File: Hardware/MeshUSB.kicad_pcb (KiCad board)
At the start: 2 copper layers, 30.4 x 40.8 mm, 33 parts, among them P1 USB_4, P2 PVCell, Q1 MOS_P, U1 XBEE, U2 AP7313-3.3VREGULATOR, U4 FT231X-SSOP, U5 LTC4070

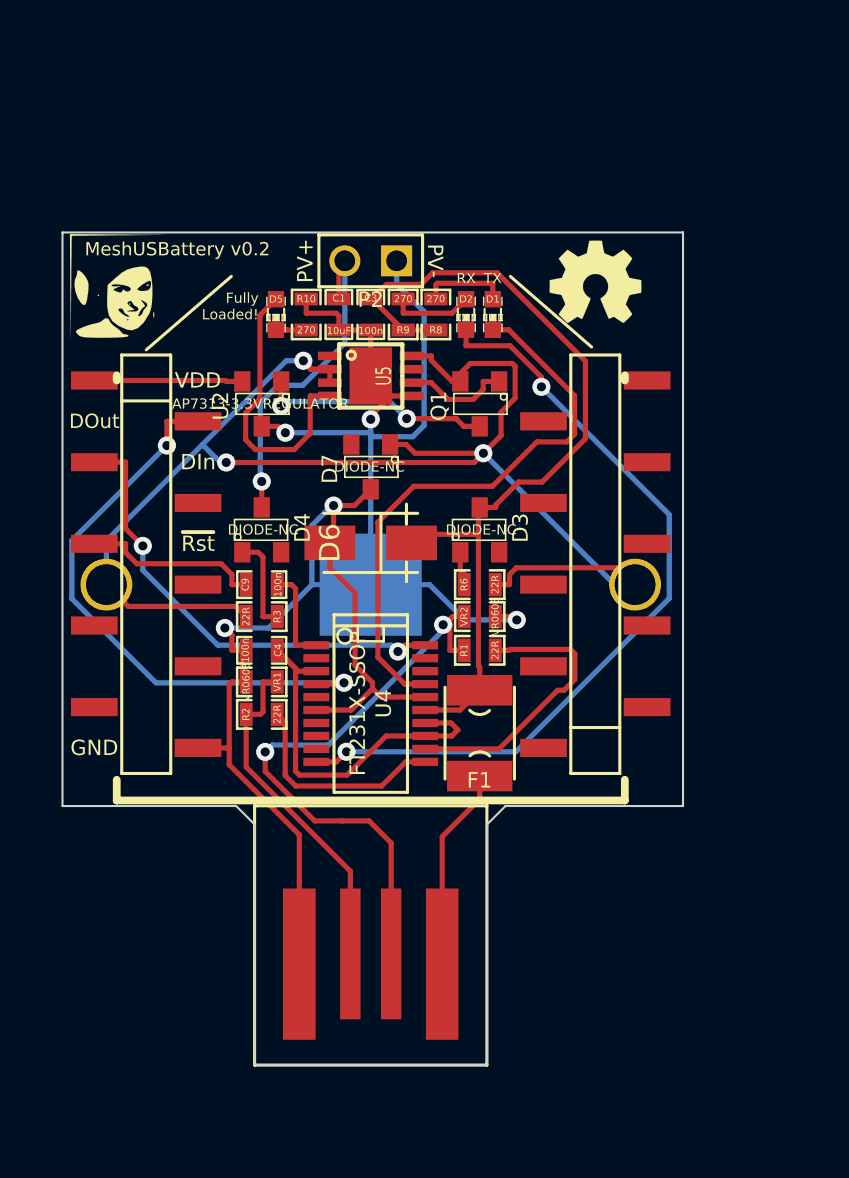
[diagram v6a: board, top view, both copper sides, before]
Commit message: Added mounting holes, some SMT jumpers and a voltage divider. Extended board for mounts by 3.5mm.
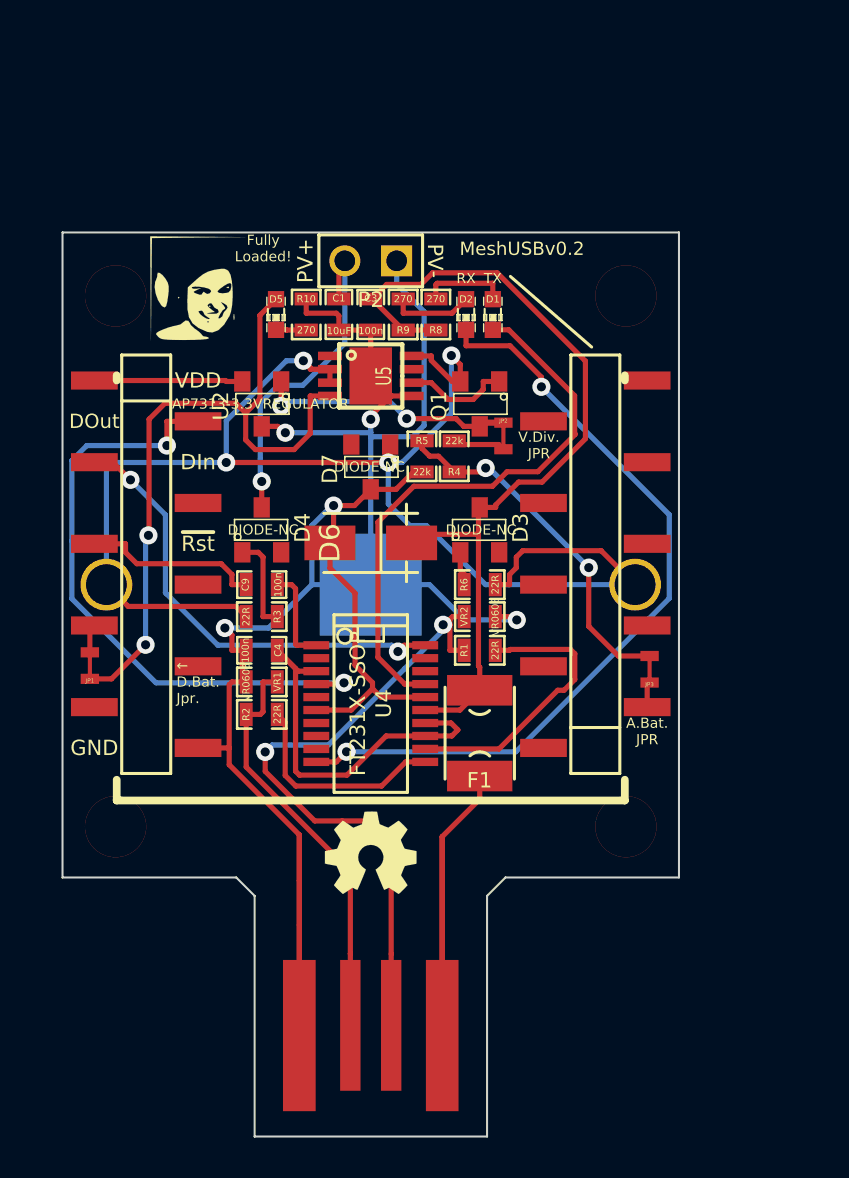
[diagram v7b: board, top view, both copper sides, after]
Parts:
- added 1PIN: P***, _MUSB_3mmTH-1pin, F.Cu at (161.2, 126.9)
- added 1PIN: P***, _MUSB_3mmTH-1pin, F.Cu at (136.0, 126.9)
- added 1PIN: P***, _MUSB_3mmTH-1pin, F.Cu at (136.0, 100.9)
- added 1PIN: P***, _MUSB_3mmTH-1pin, F.Cu at (161.0, 100.9)
- added JP1: JUMPER, _MUSB_SMTJumper, F.Cu at (134.7, 119.0)
- added JP2: JUMPER, _MUSB_SMTJumper, F.Cu at (155.0, 107.7)
- added JP3: JUMPER, _MUSB_SMTJumper, F.Cu at (162.2, 119.2)
- added R4: 22k, _MUSB_SM0603_Resistor, F.Cu at (152.6, 108.7)
- added R5: 22k, _MUSB_SM0603_Resistor, F.Cu at (151.0, 108.7)
- moved G1 30.1 mm to (148.5, 128.1)
- moved G0 3.93 mm to (140.0, 100.5)
- moved P1 3.50 mm to (148.5, 135.7)
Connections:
- D5 pad 1: N-0000026 (its old number) -> _MT_PB4
- U5 pad 4: N-0000026 (its old number) -> _MT_PB4
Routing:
- net N-0000019: track 0.00 -> 33.1 mm, vias 0 -> 2
- net _MT_PF7: track 0.00 -> 17.7 mm, vias 0 -> 2
- net N-0000026 (its old number): track 14.0 -> 0.00 mm
- net GND: track 96.2 -> 108.9 mm
- net N-0000064: track 9.98 -> 19.7 mm
- net N-0000058: track 16.9 -> 20.4 mm
- net N-0000057: track 28.8 -> 32.3 mm
- net N-0000016: track 0.00 -> 2.58 mm
- net N-0000011: track 28.6 -> 30.9 mm
- net _MT_PB4: track 0.00 -> 2.08 mm
- net N-0000017: track 11.5 -> 12.8 mm
- net N-0000021: track 0.00 -> 1.09 mm
- net N-0000030: track 73.5 -> 73.2 mm, vias 3 -> 4
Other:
- board size 30.4 x 40.8 mm -> 30.2 x 44.3 mm
- board text added: "A.Bat. JPR"
- board text added: "MeshUSBv0.2"
- board text added: "V.Div. JPR"
- board text added: "← D.Bat. Jpr."
- board text removed: "MeshUSBattery v0.2"

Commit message: Change all the things\!
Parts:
- moved JP1 29.8 mm to (162.0, 107.0)
- moved JP3 8.12 mm to (162.0, 111.0)
- moved U2 7.13 mm to (148.5, 110.9)
- moved R4 6.53 mm to (146.1, 109.1)
- moved JP2 6.53 mm to (148.5, 108.3), turned to 180 degrees
- moved D7 6.22 mm to (143.2, 112.4), turned to 0 degrees
- moved D4 5.32 mm to (143.0, 107.0), turned to 270 degrees
- moved D6 1.17 mm to (148.5, 114.1)
- moved Q1 0.87 mm to (154.0, 107.0), turned to 90 degrees
- moved R5 0.38 mm to (150.9, 109.1)
- moved D3 0.10 mm to (153.8, 112.4)
- renumbered 1PIN to 1PIN1, 1PIN to 1PIN2, 1PIN to 1PIN3, 1PIN to 1PIN4
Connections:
- net _MT_PF7 renamed _MT_PF3
- D5 pad 1: _MT_PB4 -> _MT_PF2
- H1 pad 7: N-0000019 (its old number) -> N-0000022
- H2 pad 7: N-0000069 (its old number) -> N-0000023
- H2 pad 8: N-0000068 (its old number) -> N-0000020
- JP1 pad 1: _MT_PB4 -> N-0000020
- JP1 pad 2: N-0000019 (its old number) -> _MT_PF2
- JP3 pad 1: N-0000021 -> N-0000023
- U5 pad 4: _MT_PB4 -> _MT_PF2
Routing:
- net N-0000019 (its old number): track 33.1 -> 0.00 mm, vias 2 -> 0
- net _MT_PF2: track 0.00 -> 33.1 mm, vias 0 -> 2
- net N-000007: track 30.9 -> 17.4 mm, vias 2 -> 0
- net N-0000035: track 4.73 -> 16.4 mm
- net N-0000017: track 12.8 -> 1.68 mm, vias 2 -> 0
- net _MT_PF3: track 17.7 -> 27.1 mm
- net BAT+: track 7.27 -> 16.5 mm
- net N-0000061: track 19.7 -> 13.5 mm
- net N-0000010: track 22.4 -> 28.0 mm
- net N-0000032: track 73.2 -> 78.6 mm, vias 4 -> 3
- net N-0000016: track 2.58 -> 7.42 mm
- net N-0000023: track 0.00 -> 3.49 mm
- net N-0000036: track 16.5 -> 13.1 mm, vias 1 -> 0
- net GND: track 108.9 -> 112.3 mm, vias 5 -> 3
- net USB_VDD: track 42.6 -> 45.6 mm
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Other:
- net class Default: clearance 0.254 -> 0.2032; trace_width 0.254 -> 0.2032
- rule pad_to_mask_clearance: 0 -> 0.2032
- rule trace_clearance: 0.254 -> 0.2032
- rule trace_min: 0.254 -> 0.2032
- board text added: "A.Bat. JPR →"
- board text added: "D.Bat. Jpr. →"
- board text removed: "A.Bat. JPR"
- board text removed: "← D.Bat. Jpr."
